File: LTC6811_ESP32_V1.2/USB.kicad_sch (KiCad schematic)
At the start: 11 parts, among them J8 SERIAL /NC, U10 CP2104

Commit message: Add files via upload
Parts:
- C40: value 2.2uF 16V -> 4.7uF 16V; Link https://www.digikey.jp/en/products/detail/kemet/C0603C225K4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 -> https://www.digikey.jp/en/products/detail/samsung-electro-m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; MPN C0603C225K4PAC7867 -> CL10A475KO8NNNC
- J8: footprint Connector_PinHeader_2.54mm:PinHeader_1x05_P2.54mm_Vertical -> Connector_PinHeader_2.54mm:PinHeader_1x04_P2.54mm_Vertical; symbol BMS-Master-rescue:Conn_01x05-Connector_Generic-BMS-Master-rescue -> Connector_Generic:Conn_01x04
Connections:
- net +3V3: now also J8.4 (Pin_4); no longer J8.5 (Pin_5)
- no-connect marks 14 -> 13
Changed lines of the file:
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@@
   (junction (at 105.41 94.615) (diameter 0) (color 0 0 0 0)
   )
+  (junction (at 44.45 59.055) (diameter 0) (color 0 0 0 0)
+  )
+  (junction (at 146.05 59.055) (diameter 0) (color 0 0 0 0)
+  )
+  (junction (at 143.51 38.735) (diameter 0) (color 0 0 0 0)
+  )
+  (junction (at 106.68 31.75) (diameter 0) (color 0 0 0 0)
+  )
+  (junction (at 125.73 43.815) (diameter 0) (color 0 0 0 0)
+  )
+  (junction (at 157.48 38.735) (diameter 0) (color 0 0 0 0)
+  )
   (junction (at 80.01 31.75) (diameter 0) (color 0 0 0 0)
-  )
-  (junction (at 44.45 59.055) (diameter 0) (color 0 0 0 0)
-  )
-  (junction (at 146.05 59.055) (diameter 0) (color 0 0 0 0)
-  )
-  (junction (at 143.51 38.735) (diameter 0) (color 0 0 0 0)
-  )
-  (junction (at 106.68 31.75) (diameter 0) (color 0 0 0 0)
-  )
-  (junction (at 125.73 43.815) (diameter 0) (color 0 0 0 0)
-  )
-  (junction (at 157.48 38.735) (diameter 0) (color 0 0 0 0)
   )
   (no_connect (at 88.9 48.895))
@@
   (no_connect (at 88.9 74.295))
   (no_connect (at 124.46 69.215))
-  (no_connect (at 49.53 84.455))
   (no_connect (at 124.46 64.135))
   (no_connect (at 101.6 36.195))
@@
     (stroke (width 0) (type default))
   )
-  (wire (pts (xy 44.45 86.995) (xy 44.45 59.055))
+  (wire (pts (xy 44.45 84.455) (xy 44.45 59.055))
     (stroke (width 0) (type default))
   )
@@
     (stroke (width 0) (type default))
   )
-  (wire (pts (xy 41.91 56.515) (xy 41.91 89.535))
+  (wire (pts (xy 41.91 56.515) (xy 41.91 86.995))
     (stroke (width 0) (type default))
   )
@@
     (stroke (width 0) (type default))
   )
-  (wire (pts (xy 48.26 98.425) (xy 48.26 92.075))
+  (wire (pts (xy 48.26 90.805) (xy 48.26 89.535))
     (stroke (width 0) (type default))
   )
@@
     (stroke (width 0) (type default))
   )
-  (wire (pts (xy 48.26 92.075) (xy 49.53 92.075))
+  (wire (pts (xy 48.26 89.535) (xy 49.53 89.535))
     (stroke (width 0) (type default))
   )
@@
     (stroke (width 0) (type default))
   )
-  (wire (pts (xy 41.91 89.535) (xy 49.53 89.535))
+  (wire (pts (xy 41.91 86.995) (xy 49.53 86.995))
     (stroke (width 0) (type default))
   )
@@
     (stroke (width 0) (type default))
   )
-  (wire (pts (xy 49.53 86.995) (xy 44.45 86.995))
+  (wire (pts (xy 49.53 84.455) (xy 44.45 84.455))
     (stroke (width 0) (type default))
   )
@@
       (effects (font (size 1.27 1.27)) (justify left))
     )
-    (property "Value" "2.2uF 16V" (at 129.921 85.598 0)
+    (property "Value" "4.7uF 16V" (at 129.921 85.598 0)
       (effects (font (size 1.27 1.27)) (justify left))
     )
@@
       (effects (font (size 1.27 1.27)) hide)
     )
-    (property "Datasheet" "https://connect.kemet.com:7667/gateway/IntelliData-ComponentDocumentation/1.0/download/datasheet/C0603C225K4PACTU" (at 127 84.455 0)
-      (effects (font (size 1.27 1.27)) hide)
-    )
-    (property "MPN" "C0603C225K4PAC7867" (at 127 84.455 0)
-      (effects (font (size 1.27 1.27)) hide)
-    )
-    (property "Description" "2.2 µF ±10% 16V Ceramic Capacitor X5R 0603 (1608 Metric)" (at 127 84.455 0)
-      (effects (font (size 1.27 1.27)) hide)
-    )
-    (property "Link" "https://www.digikey.jp/en/products/detail/kemet/C0603C225K4PAC7867/2200308" (at 127 84.455 0)
+    (property "Datasheet" "https://mm.digikey.com/Volume0/opasdata/d220001/medias/docus/2328/CL10A475KO8NNNC_Spec.pdf" (at 127 84.455 0)
+      (effects (font (size 1.27 1.27)) hide)
+    )
+    (property "MPN" "CL10A475KO8NNNC" (at 127 84.455 0)
+      (effects (font (size 1.27 1.27)) hide)
+    )
+    (property "Description" "4.7 µF ±10% 16V Ceramic Capacitor X5R 0603 (1608 Metric)" (at 127 84.455 0)
+      (effects (font (size 1.27 1.27)) hide)
+    )
+    (property "Link" "https://www.digikey.jp/en/products/detail/samsung-electro-mechanics/CL10A475KO8NNNC/3887442" (at 127 84.455 0)
       (effects (font (size 1.27 1.27)) hide)
     )
@@
     )
   )
-  (symbol (lib_id "power:VDD") (at 80.01 31.75 0) (unit 1)
-    (in_bom yes) (on_board yes) (dnp no)
-    (property "Reference" "#PWR062" (at 80.01 35.56 0)
-      (effects (font (size 1.27 1.27)) hide)
-    )
-    (property "Value" "VDD" (at 80.4418 27.3558 0)
-      (effects (font (size 1.27 1.27)))
-    )
-    (property "Footprint" "" (at 80.01 31.75 0)
-      (effects (font (size 1.27 1.27)) hide)
-    )
-    (property "Datasheet" "" (at 80.01 31.75 0)
-      (effects (font (size 1.27 1.27)) hide)
-    )
-    (pin "1")
-    (instances
-      (project "LTC6811_ESP32_V1.2"
-        (path "/6a86ff6f-b159-4c4c-8a40-e732cc82e010/00000000-0000-0000-0000-00005c246ca0"
-          (reference "#PWR062") (unit 1)
-        )
-      )
-    )
-  )
-  (symbol (lib_id "power:VDD") (at 58.42 71.755 0) (unit 1)
-    (in_bom yes) (on_board yes) (dnp no)
-    (property "Reference" "#PWR061" (at 58.42 75.565 0)
-      (effects (font (size 1.27 1.27)) hide)
-    )
-    (property "Value" "VDD" (at 58.8518 67.3608 0)
-      (effects (font (size 1.27 1.27)))
-    )
-    (property "Footprint" "" (at 58.42 71.755 0)
-      (effects (font (size 1.27 1.27)) hide)
-    )
-    (property "Datasheet" "" (at 58.42 71.755 0)
-      (effects (font (size 1.27 1.27)) hide)
-    )
-    (pin "1")
-    (instances
-      (project "LTC6811_ESP32_V1.2"
-        (path "/6a86ff6f-b159-4c4c-8a40-e732cc82e010/00000000-0000-0000-0000-00005c246ca0"
-          (reference "#PWR061") (unit 1)
-        )
-      )
-    )
-  )
   (symbol (lib_id "BMS-Master-rescue:C-Device") (at 143.51 42.545 0) (unit 1)
     (in_bom yes) (on_board yes) (dnp no)
-    (property "Reference" "C42" (at 146.431 41.3766 0)
-      (effects (font (size 1.27 1.27)) (justify left))
-    )
-    (property "Value" "2.2uF 16V" (at 146.431 43.688 0)
+    (property "Reference" "C42" (at 143.51 40.64 0)
+      (effects (font (size 1.27 1.27)) (justify left))
+    )
+    (property "Value" "2.2uF 16V" (at 138.43 46.99 0)
       (effects (font (size 1.27 1.27)) (justify left))
     )
@@
   (symbol (lib_id "BMS-Master-rescue:C-Device") (at 133.35 42.545 0) (unit 1)
     (in_bom yes) (on_board yes) (dnp no)
-    (property "Reference" "C41" (at 136.271 41.3766 0)
-      (effects (font (size 1.27 1.27)) (justify left))
-    )
-    (property "Value" "100nF 100V" (at 136.271 43.688 0)
+    (property "Reference" "C41" (at 128.905 40.64 0)
+      (effects (font (size 1.27 1.27)) (justify left))
+    )
+    (property "Value" "100nF 100V" (at 127 45.085 0)
       (effects (font (size 1.27 1.27)) (justify left))
     )
@@
     )
   )
-  (symbol (lib_id "BMS-Master-rescue:Conn_01x05-Connector_Generic-BMS-Master-rescue") (at 54.61 86.995 0) (mirror x) (unit 1)
+  (symbol (lib_id "Connector_Generic:Conn_01x04") (at 54.61 86.995 0) (mirror x) (unit 1)
     (in_bom yes) (on_board yes) (dnp no)
     (property "Reference" "J8" (at 56.642 88.0618 0)
@@
       (effects (font (size 1.27 1.27)) (justify left))
     )
-    (property "Footprint" "Connector_PinHeader_2.54mm:PinHeader_1x05_P2.54mm_Vertical" (at 54.61 86.995 0)
-      (effects (font (size 1.27 1.27)) hide)
-    )
-    (property "Datasheet" "" (at 54.61 86.995 0)
+    (property "Footprint" "Connector_PinHeader_2.54mm:PinHeader_1x04_P2.54mm_Vertical" (at 54.61 86.995 0)
+      (effects (font (size 1.27 1.27)) hide)
+    )
+    (property "Datasheet" "~" (at 54.61 86.995 0)
       (effects (font (size 1.27 1.27)) hide)
     )
@@
     (pin "3")
     (pin "4")
-    (pin "5")
     (instances
       (project "LTC6811_ESP32_V1.2"
@@
     )
   )
-  (symbol (lib_id "power:GND") (at 48.26 98.425 0) (unit 1)
-    (in_bom yes) (on_board yes) (dnp no)
-    (property "Reference" "#PWR059" (at 48.26 104.775 0)
-      (effects (font (size 1.27 1.27)) hide)
-    )
-    (property "Value" "GND" (at 48.387 102.8192 0)
-      (effects (font (size 1.27 1.27)))
-    )
-    (property "Footprint" "" (at 48.26 98.425 0)
-      (effects (font (size 1.27 1.27)) hide)
-    )
-    (property "Datasheet" "" (at 48.26 98.425 0)
+  (symbol (lib_id "power:GND") (at 48.26 90.805 0) (unit 1)
+    (in_bom yes) (on_board yes) (dnp no)
+    (property "Reference" "#PWR059" (at 48.26 97.155 0)
+      (effects (font (size 1.27 1.27)) hide)
+    )
+    (property "Value" "GND" (at 48.26 94.615 0)
+      (effects (font (size 1.27 1.27)))
+    )
+    (property "Footprint" "" (at 48.26 90.805 0)
+      (effects (font (size 1.27 1.27)) hide)
+    )
+    (property "Datasheet" "" (at 48.26 90.805 0)
       (effects (font (size 1.27 1.27)) hide)
     )
@@
         )
       )
+    )
+  )
+  (symbol (lib_id "power:VDD") (at 58.42 71.755 0) (unit 1)
+    (in_bom yes) (on_board yes) (dnp no) (fields_autoplaced)
+    (property "Reference" "#PWR041" (at 58.42 75.565 0)
+      (effects (font (size 1.27 1.27)) hide)
+    )
+    (property "Value" "VDD" (at 58.42 66.675 0)
+      (effects (font (size 1.27 1.27)))
+    )
+    (property "Footprint" "" (at 58.42 71.755 0)
+      (effects (font (size 1.27 1.27)) hide)
+    )
+    (property "Datasheet" "" (at 58.42 71.755 0)
+      (effects (font (size 1.27 1.27)) hide)
+    )
+    (pin "1")
+    (instances
+      (project "LTC6811_ESP32_V1.2"
+        (path "/6a86ff6f-b159-4c4c-8a40-e732cc82e010/00000000-0000-0000-0000-00005c246ca0"
+          (reference "#PWR041") (unit 1)
+        )
+      )
+    )
+  )
+  (symbol (lib_id "power:VDD") (at 80.01 31.75 0) (unit 1)
+    (in_bom yes) (on_board yes) (dnp no) (fields_autoplaced)
+    (property "Reference" "#PWR044" (at 80.01 35.56 0)
+      (effects (font (size 1.27 1.27)) hide)
+    )
+    (property "Value" "VDD" (at 80.01 26.67 0)
+      (effects (font (size 1.27 1.27)))
+    )
+    (property "Footprint" "" (at 80.01 31.75 0)
+      (effects (font (size 1.27 1.27)) hide)
+    )
+    (property "Datasheet" "" (at 80.01 31.75 0)
+      (effects (font (size 1.27 1.27)) hide)
+    )
+    (pin "1")
+    (instances
+      (project "LTC6811_ESP32_V1.2"
+        (path "/6a86ff6f-b159-4c4c-8a40-e732cc82e010/00000000-0000-0000-0000-00005c246ca0"
+          (reference "#PWR044") (unit 1)
+        )
+      )

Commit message: Add files via upload
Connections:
- net +3V3: now also J8.1 (Pin_1); no longer J8.4 (Pin_4)
- net GND: now also J8.4 (Pin_4); no longer J8.1 (Pin_1)
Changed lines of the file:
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@@
     (company "teTra")
   )
+  (junction (at 46.99 56.515) (diameter 0) (color 0 0 0 0)
+  )
   (junction (at 133.35 38.735) (diameter 0) (color 0 0 0 0)
   )
   (junction (at 140.97 56.515) (diameter 0) (color 0 0 0 0)
-  )
-  (junction (at 41.91 56.515) (diameter 0) (color 0 0 0 0)
   )
   (junction (at 105.41 94.615) (diameter 0) (color 0 0 0 0)
@@
     (stroke (width 0) (type default))
   )
-  (wire (pts (xy 44.45 84.455) (xy 44.45 59.055))
+  (wire (pts (xy 44.45 86.995) (xy 44.45 59.055))
     (stroke (width 0) (type default))
   )
@@
     (stroke (width 0) (type default))
   )
-  (wire (pts (xy 41.91 56.515) (xy 41.91 86.995))
+  (wire (pts (xy 46.99 84.455) (xy 46.99 56.515))
     (stroke (width 0) (type default))
   )
@@
     (stroke (width 0) (type default))
   )
+  (wire (pts (xy 46.99 56.515) (xy 66.04 56.515))
+    (stroke (width 0) (type default))
+  )
   (wire (pts (xy 73.66 56.515) (xy 88.9 56.515))
     (stroke (width 0) (type default))
@@
     (stroke (width 0) (type default))
   )
-  (wire (pts (xy 38.1 56.515) (xy 41.91 56.515))
+  (wire (pts (xy 38.1 56.515) (xy 46.99 56.515))
     (stroke (width 0) (type default))
   )
@@
     (stroke (width 0) (type default))
   )
+  (wire (pts (xy 49.53 84.455) (xy 46.99 84.455))
+    (stroke (width 0) (type default))
+  )
   (wire (pts (xy 124.46 48.895) (xy 125.73 48.895))
     (stroke (width 0) (type default))
@@
     (stroke (width 0) (type default))
   )
-  (wire (pts (xy 41.91 56.515) (xy 66.04 56.515))
-    (stroke (width 0) (type default))
-  )
-  (wire (pts (xy 41.91 86.995) (xy 49.53 86.995))
-    (stroke (width 0) (type default))
-  )
   (wire (pts (xy 124.46 59.055) (xy 146.05 59.055))
     (stroke (width 0) (type default))
@@
     (stroke (width 0) (type default))
   )
-  (wire (pts (xy 49.53 84.455) (xy 44.45 84.455))
+  (wire (pts (xy 49.53 86.995) (xy 44.45 86.995))
     (stroke (width 0) (type default))
   )
@@
     )
   )
-  (symbol (lib_id "Connector_Generic:Conn_01x04") (at 54.61 86.995 0) (mirror x) (unit 1)
-    (in_bom yes) (on_board yes) (dnp no)
-    (property "Reference" "J8" (at 56.642 88.0618 0)
-      (effects (font (size 1.27 1.27)) (justify left))
-    )
-    (property "Value" "SERIAL /NC" (at 56.642 85.7504 0)
-      (effects (font (size 1.27 1.27)) (justify left))
-    )
-    (property "Footprint" "Connector_PinHeader_2.54mm:PinHeader_1x04_P2.54mm_Vertical" (at 54.61 86.995 0)
-      (effects (font (size 1.27 1.27)) hide)
-    )
-    (property "Datasheet" "~" (at 54.61 86.995 0)
-      (effects (font (size 1.27 1.27)) hide)
-    )
-    (property "MPN" "70543-0004" (at 54.61 86.995 0)
-      (effects (font (size 1.27 1.27)) hide)
-    )
+  (symbol (lib_id "Connector_Generic:Conn_01x04") (at 54.61 84.455 0) (unit 1)
+    (in_bom yes) (on_board yes) (dnp no)
+    (property "Reference" "J8" (at 56.642 83.3882 0)
+      (effects (font (size 1.27 1.27)) (justify left))
+    )
+    (property "Value" "SERIAL /NC" (at 56.642 85.6996 0)
+      (effects (font (size 1.27 1.27)) (justify left))
+    )
+    (property "Footprint" "Connector_PinHeader_2.54mm:PinHeader_1x04_P2.54mm_Vertical" (at 54.61 84.455 0)
+      (effects (font (size 1.27 1.27)) hide)
+    )
+    (property "Datasheet" "~" (at 54.61 84.455 0)
+      (effects (font (size 1.27 1.27)) hide)
+    )
+    (property "MPN" "70543-0004" (at 54.61 84.455 0)
+      (effects (font (size 1.27 1.27)) hide)
+    )

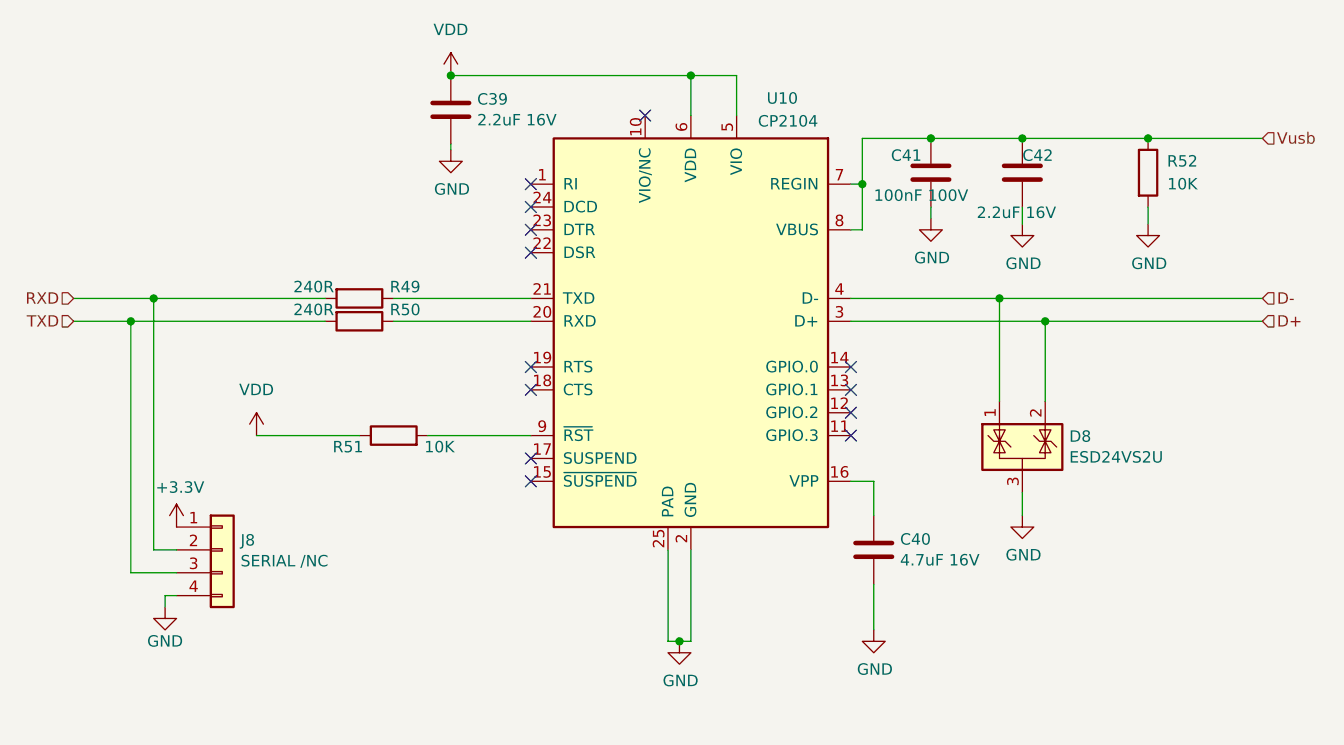
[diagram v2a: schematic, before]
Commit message: add BOM
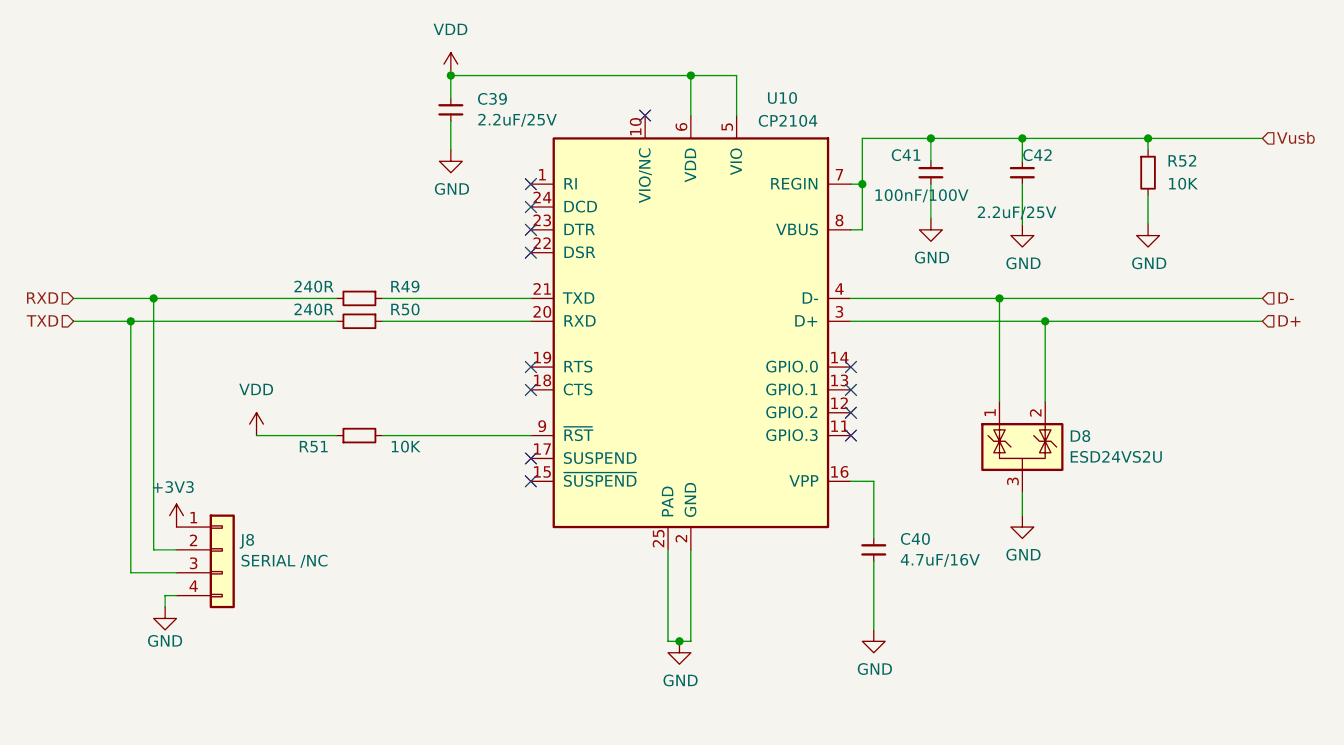
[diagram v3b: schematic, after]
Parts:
- C39, C42: value 2.2uF 16V -> 2.2uF/25V; symbol BMS-Master-rescue:C-Device -> Device:C; Link https://www.digikey.jp/en/products/detail/kemet/C0603C225K4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 -> https://www.digikey.jp/en/products/detail/murata-electronic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; MPN C0603C225K4PAC7867 -> GRM188R61E225KA12D
- C40: value 4.7uF 16V -> 4.7uF/16V; symbol BMS-Master-rescue:C-Device -> Device:C
- C41: value 100nF 100V -> 100nF/100V; symbol BMS-Master-rescue:C-Device -> Device:C
- J8: Link (none) -> https://www.digikey.jp/en/products/detail/amphenol-cs-comme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; MPN 70543-0004 -> G800W304018EU
- R49, R50, R51, R52: symbol Device:R -> Device:R_Small
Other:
- moved on the sheet: R51
